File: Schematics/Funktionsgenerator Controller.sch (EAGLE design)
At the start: 37 parts, among them IC1 ATMEGA328PB-AU, IC2 TLE4270-2D, IC3 AD9833BRMZ, IC4 LM318D, IC5 LM318D, X1 22-23-2051, X2 ENCODER-SWITCH, X3 22-23-2031, X4 22-23-2031, X5 22-23-2031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

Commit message: Added Resistor to limit current for TFT Backlight
Das TFT Display wurde zu heiß, da der Vorwiderstand für die Hintergrundbeleuchtung des TFT lediglich 6Ohm beträgt. Durch einen weiteren Vorwiderstand von 22Ohm konnte die Wärmeentwicklung des Displays erheblich reduziert werden ohne eine merkliche Reduzierung der Helligkeit. Alternativ wäre zu überlegen ob ein Trimmer zur Justierung eingebaut werden sollte
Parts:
- removed C3: EEEFT1V470AR, SamacSys_Parts:EEEFT1V470AR
- added C15: TAJD476K010R, SamacSys_Parts:TAJD476K010R
- added R7: 22, resistor:R-EU_R0603
- C1, C11, C12, C13, C14, C7, C8: value 100nF -> 100n
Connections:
- new net N$18: P1.LED_+, R7.1
- net GND: now also C15.-; no longer C3.+
- net VCC: now also C15.+, R7.2; no longer C3.-, P1.LED_+
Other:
- moved on the sheet: C10, C11, C12, C13, C14, C2, C6, C7, C8, C9, IC2, IC3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

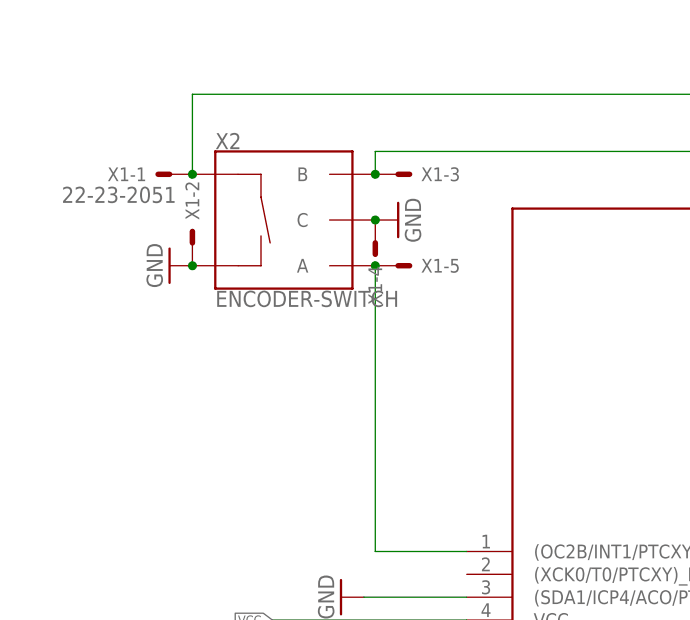
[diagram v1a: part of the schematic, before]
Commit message: VCC on encoder connector for external pull-up
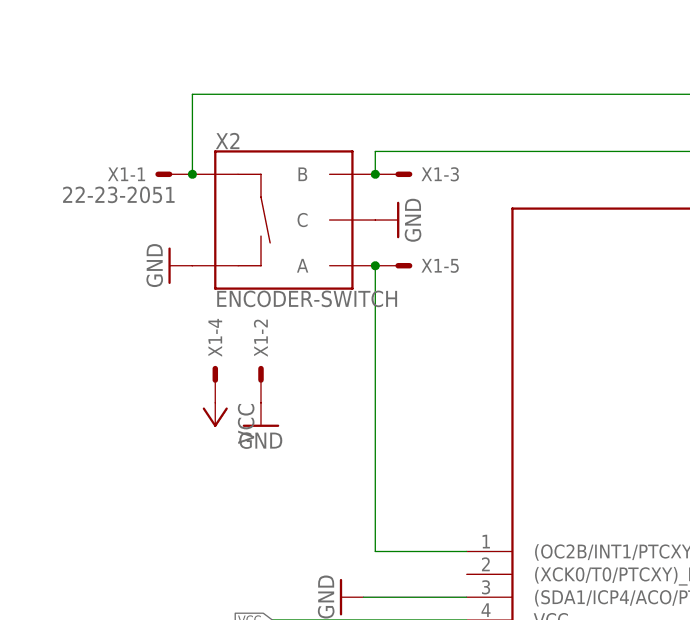
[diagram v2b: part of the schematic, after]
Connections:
- net GND: no longer X1-4.S
- net VCC: now also X1-4.S
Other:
- moved on the sheet: X1-2, X1-4
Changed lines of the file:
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@@
 <part name="GND19" library="supply1" library_urn="urn:adsk.eagle:library:371" deviceset="GND" device=""/>
 <part name="R7" library="resistor" library_urn="urn:adsk.eagle:library:348" deviceset="R-EU_" device="R0603" package3d_urn="urn:adsk.eagle:package:26057/1" value="22"/>
+<part name="GND8" library="supply1" library_urn="urn:adsk.eagle:library:371" deviceset="GND" device=""/>
+<part name="P+1" library="supply1" library_urn="urn:adsk.eagle:library:371" deviceset="VCC" device=""/>
 </parts>
 <sheets>
@@
 <instance part="GND1" gate="1" x="-12.7" y="111.76" rot="R270"/>
 <instance part="X1" gate="-1" x="-12.7" y="121.92" rot="R180"/>
-<instance part="X1" gate="-2" x="-10.16" y="114.3" rot="R90"/>
+<instance part="X1" gate="-2" x="-2.54" y="99.06" rot="R90"/>
 <instance part="X1" gate="-3" x="12.7" y="121.92"/>
-<instance part="X1" gate="-4" x="10.16" y="114.3" rot="R270"/>
+<instance part="X1" gate="-4" x="-7.62" y="99.06" rot="R90"/>
 <instance part="X1" gate="-5" x="12.7" y="111.76"/>
 <instance part="P3" gate="G$1" x="210.82" y="212.09" rot="R270"/>
@@
 <instance part="GND19" gate="1" x="172.72" y="88.9"/>
 <instance part="R7" gate="G$1" x="256.54" y="35.56"/>
+<instance part="GND8" gate="1" x="-2.54" y="93.98"/>
+<instance part="P+1" gate="VCC" x="-7.62" y="93.98" rot="R180"/>
 </instances>
 <busses>
@@
 <label x="264.16" y="35.56" size="1.016" layer="95" xref="yes"/>
 </segment>
+<segment>
+<pinref part="X1" gate="-4" pin="S"/>
+<pinref part="P+1" gate="VCC" pin="VCC"/>
+</segment>
 </net>
 <net name="GND" class="0">
@@
 <segment>
 <pinref part="GND5" gate="1" pin="GND"/>
-<pinref part="X1" gate="-4" pin="S"/>
 <pinref part="X2" gate="G$1" pin="C"/>
-<junction x="10.16" y="116.84"/>
 </segment>
 <segment>
 <pinref part="GND1" gate="1" pin="GND"/>
-<pinref part="X1" gate="-2" pin="S"/>
 <pinref part="X2" gate="G$1" pin="SW-"/>
-<junction x="-10.16" y="111.76"/>
 </segment>
 <segment>
@@
 <pinref part="GND19" gate="1" pin="GND"/>
 </segment>
+<segment>
+<pinref part="GND8" gate="1" pin="GND"/>
+<pinref part="X1" gate="-2" pin="S"/>
+</segment>
 </net>

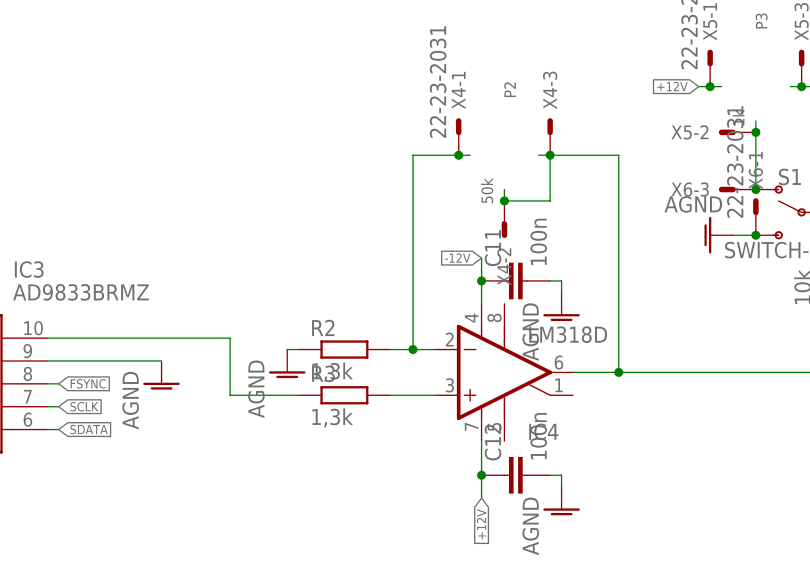
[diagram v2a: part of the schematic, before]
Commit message: moved labels on, added net names
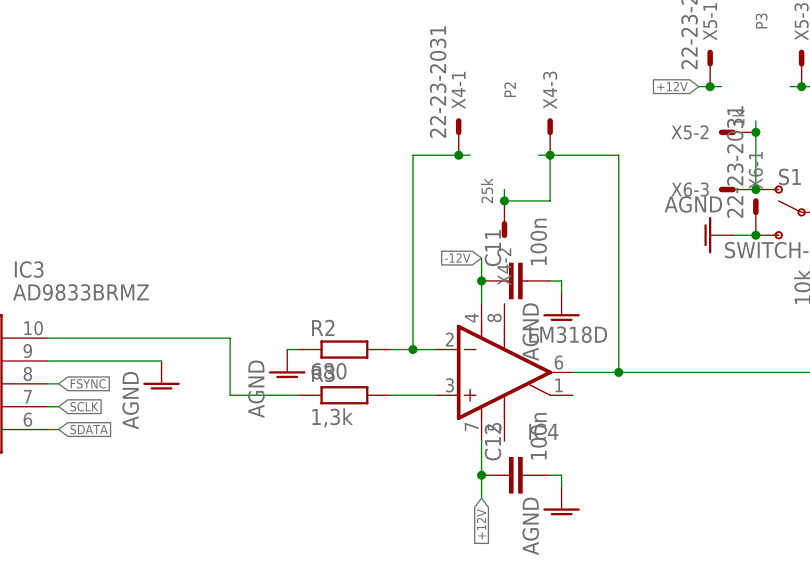
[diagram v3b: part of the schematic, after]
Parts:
- R2: value 1,3k -> 680
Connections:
- net N$12 renamed ROT_BTN
- net N$13 renamed ROT_B
- net N$14 renamed ROT_A
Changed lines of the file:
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@@
 <part name="IC4" library="linear" library_urn="urn:adsk.eagle:library:262" deviceset="LM318" device="D" package3d_urn="urn:adsk.eagle:package:16404/2" value="LM318D"/>
 <part name="R3" library="resistor" library_urn="urn:adsk.eagle:library:348" deviceset="R-EU_" device="R0603" package3d_urn="urn:adsk.eagle:package:26057/1" value="1,3k"/>
-<part name="R2" library="resistor" library_urn="urn:adsk.eagle:library:348" deviceset="R-EU_" device="R0603" package3d_urn="urn:adsk.eagle:package:26057/1" value="1,3k"/>
+<part name="R2" library="resistor" library_urn="urn:adsk.eagle:library:348" deviceset="R-EU_" device="R0603" package3d_urn="urn:adsk.eagle:package:26057/1" value="680"/>
 <part name="R5" library="resistor" library_urn="urn:adsk.eagle:library:348" deviceset="R-EU_" device="R0603" package3d_urn="urn:adsk.eagle:package:26057/1" value="10k"/>
 <part name="AGND2" library="supply1" library_urn="urn:adsk.eagle:library:371" deviceset="AGND" device=""/>
@@
 <part name="P3" library="Symbols-Not-On-Board" deviceset="POT-NOT-ON-BOARD" device="" value="1k"/>
 <part name="BU1" library="Symbols-Not-On-Board" deviceset="BNC-BUCHSE-NOT-ON-BOARD" device=""/>
-<part name="P2" library="Symbols-Not-On-Board" deviceset="POT-NOT-ON-BOARD" device="" value="50k"/>
+<part name="P2" library="Symbols-Not-On-Board" deviceset="POT-NOT-ON-BOARD" device="" value="25k"/>
 <part name="S1" library="Symbols-Not-On-Board" deviceset="SWITCH-SPDT" device=""/>
 <part name="X2" library="Symbols-Not-On-Board" deviceset="ENCODER-SWITCH" device=""/>
@@
 </segment>
 </net>
-<net name="N$12" class="0">
+<net name="ROT_BTN" class="0">
 <segment>
 <wire x1="-10.16" y1="121.92" x2="-10.16" y2="130.81" width="0.1524" layer="91"/>
@@
 </segment>
 </net>
-<net name="N$13" class="0">
+<net name="ROT_B" class="0">
 <segment>
 <pinref part="IC1" gate="G$1" pin="PD2_(PTCXY/INT0/OC3B/OC4B)"/>
@@
 </segment>
 </net>
-<net name="N$14" class="0">
+<net name="ROT_A" class="0">
 <segment>
 <pinref part="IC1" gate="G$1" pin="(OC2B/INT1/PTCXY)_PD3"/>

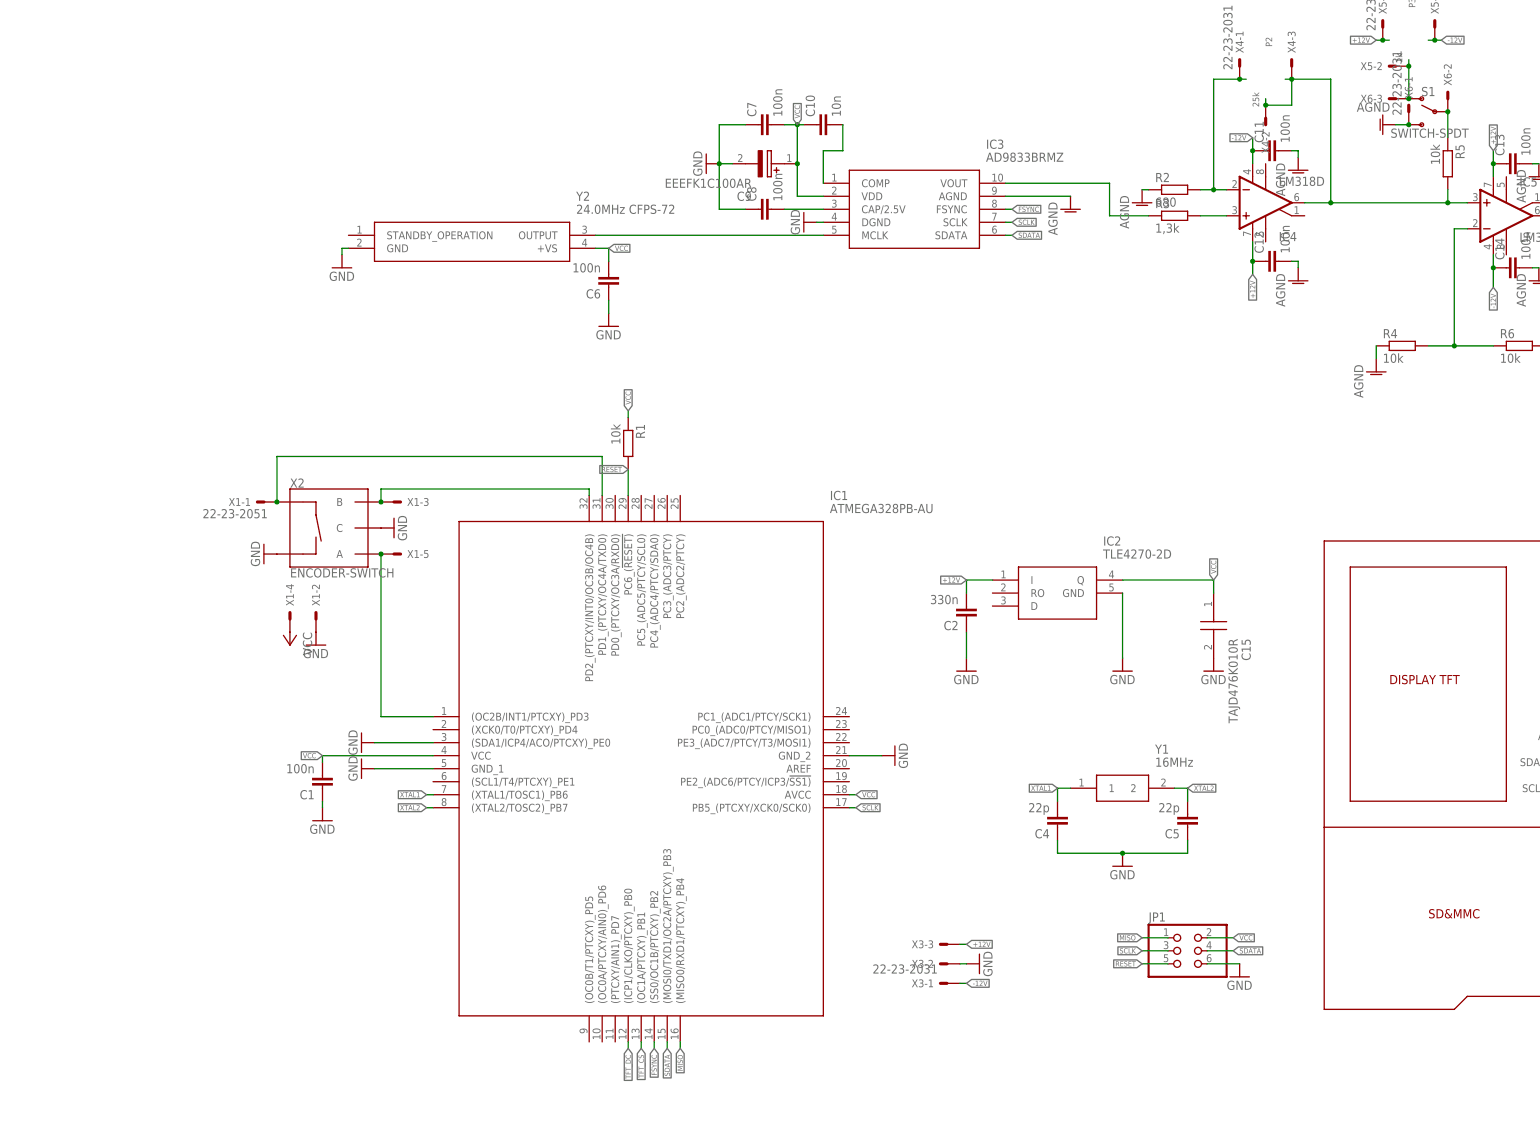
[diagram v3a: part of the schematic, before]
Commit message: Added trimmer for offset adjustment and some fixes
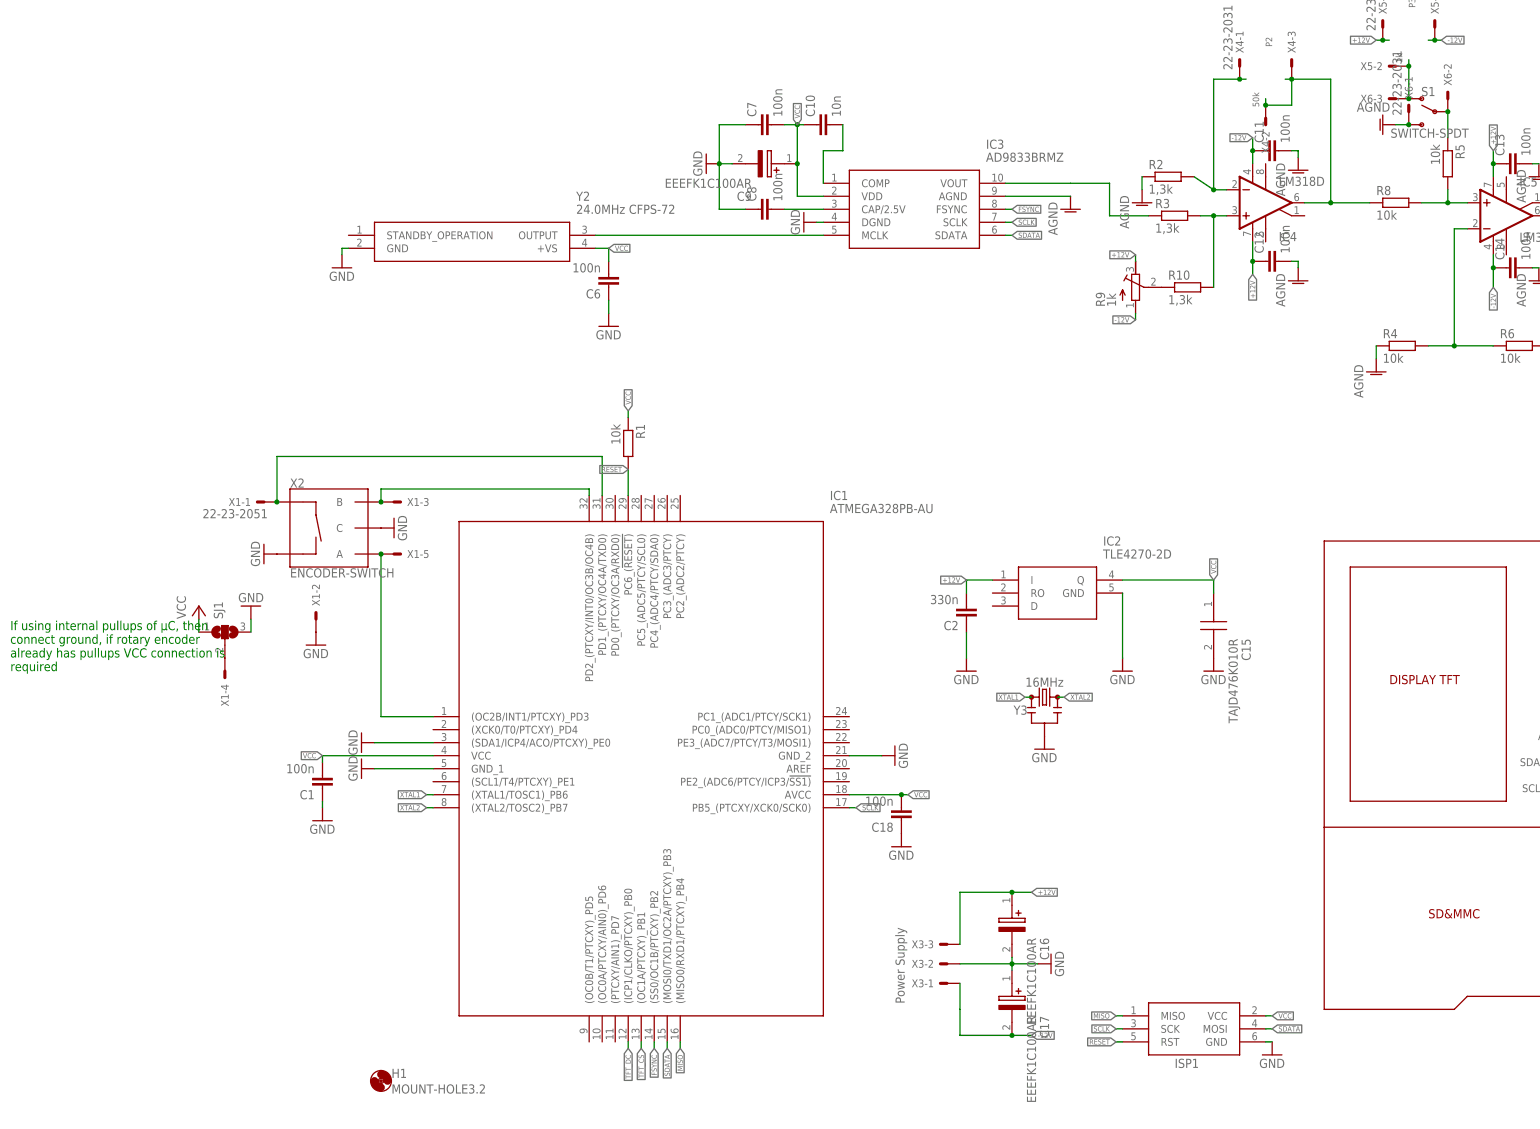
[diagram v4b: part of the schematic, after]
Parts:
- removed C4, C5: 22p, resistor:C-EUC0603
- removed JP1: (no value), pinhead:PINHD-2X3
- removed Y1: 16MHz, SamacSys_Parts:QCS16.0000F18B23M
- added C16, C17: EEEFK1C100AR, SamacSys_Parts:EEEFK1C100AR
- added C18: 100n, resistor:C-EUC0603
- added H1: MOUNT-HOLE3.2, holes:MOUNT-HOLE3.2
- added ISP1: AVRISP-6, adafruit:AVRISP-6
- added R10: 1,3k, resistor:R-EU_R0603
- added R8: 10k, resistor:R-EU_R0603
- added R9: 1k, user:EVM3ESX50B
- added SJ1: (no value), jumper:SJ2W
- added Y3: 16MHz, SparkFun-Clocks:RESONATOR-16MHZSMD_3.2X1.3
- R2: value 680 -> 1,3k
- X3: value 22-23-2031 -> Power Supply
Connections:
- new net N$12: SJ1.2, X1-4.S
- new net N$13: IC5.+IN, R5.2, R8.2
- new net N$14: R10.1, R9.S
- net +12V: now also C16.+, R9.E
- net -12V: now also C17.-, R9.A
- net GND: now also C16.-, C17.+, C18.1, ISP1.GND, SJ1.3, Y3.2; no longer C4.1, C5.1, JP1.6
- net MISO: now also ISP1.MISO; no longer JP1.1
- net N$3: now also R10.2
- net N$9: now also R8.1; no longer IC5.+IN, R5.2
- net RESET: now also ISP1.RST; no longer JP1.5
- net SCLK: now also ISP1.SCK; no longer JP1.3
- net SDATA: now also ISP1.MOSI; no longer JP1.4
- net VCC: now also C18.2, ISP1.VCC, SJ1.1; no longer JP1.2, X1-4.S
- net XTAL1: now also Y3.1; no longer C4.2, Y1.1
- net XTAL2: now also Y3.3; no longer C5.2, Y1.2
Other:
- note added: "If using internal pullups of µC, then connect ground, if rotary encoder already has pullups VCC connection is required"
- moved on the sheet: R2, X1-4
